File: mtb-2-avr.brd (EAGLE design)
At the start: 27 x 22 mm, 15 parts, among them IC1 MEGA8A-AU, Q1 14.745 MHz

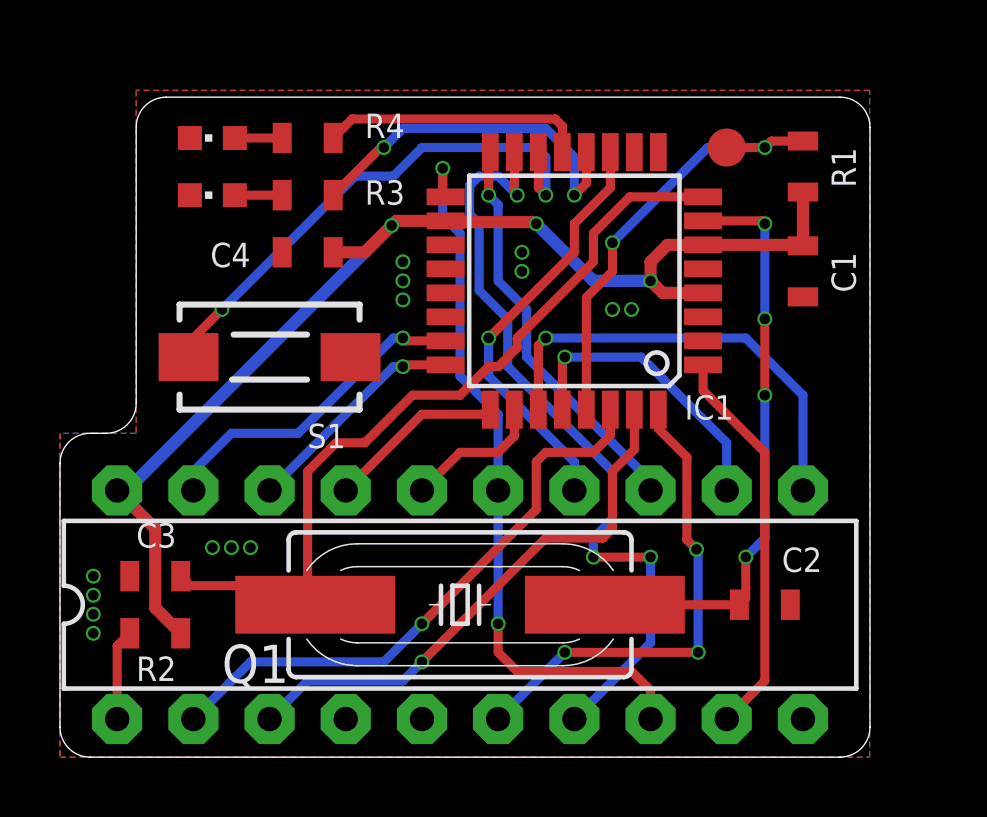
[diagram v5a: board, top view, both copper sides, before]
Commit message: Add test pad.
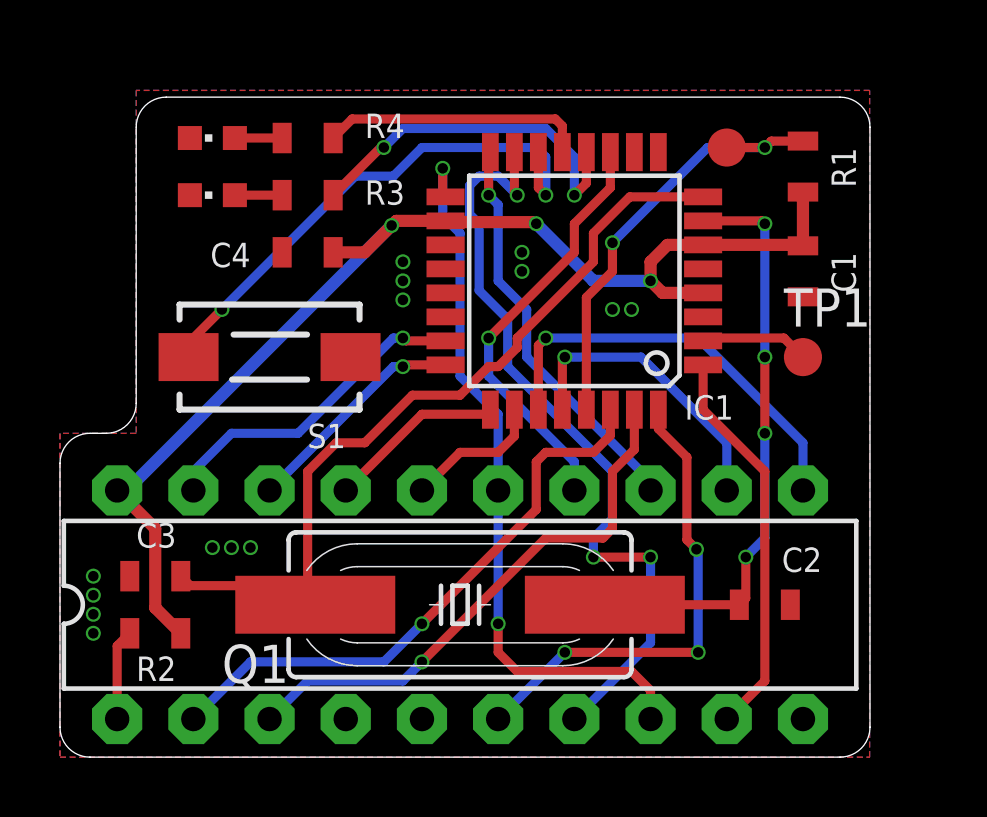
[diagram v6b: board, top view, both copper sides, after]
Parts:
- added TP1: PTR1B1,27, testpad:B1,27
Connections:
- new net TEST1: IC1.2, TP1.TP
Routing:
- net TEST1: track 0.00 -> 3.63 mm
- net SDA: track 15.0 -> 14.1 mm
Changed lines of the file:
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@@
 <layer number="25" name="tNames" color="7" fill="1" visible="no" active="yes"/>
 <layer number="26" name="bNames" color="7" fill="1" visible="no" active="yes"/>
-<layer number="27" name="tValues" color="7" fill="1" visible="yes" active="yes"/>
+<layer number="27" name="tValues" color="7" fill="1" visible="no" active="yes"/>
 <layer number="28" name="bValues" color="7" fill="1" visible="no" active="yes"/>
 <layer number="29" name="tStop" color="7" fill="3" visible="no" active="yes"/>
@@
 <attribute name="VALUE" x="9.2075" y="11.1125" size="0.8128" layer="27" rot="R180"/>
 </element>
+<element name="TP1" library="testpad" library_urn="urn:adsk.eagle:library:385" package="B1,27" package3d_urn="urn:adsk.eagle:package:27944/2" value="PTR1B1,27" x="24.765" y="13.335" smashed="yes">
+<attribute name="NAME" x="24.13" y="14.351" size="1.27" layer="25" ratio="10"/>
+<attribute name="POPULARITY" value="2" x="24.765" y="13.335" size="1.778" layer="27" display="off"/>
+<attribute name="TP_SIGNAL_NAME" value="" x="24.765" y="13.335" size="1.778" layer="27" display="off"/>
+<attribute name="VALUE" x="24.13" y="12.573" size="0.0254" layer="27"/>
+</element>
 </elements>
 <signals>
@@
 <wire x1="3.175" y1="7.62" x2="3.175" y2="4.9775" width="0.4064" layer="1"/>
 <wire x1="24.765" y1="18.835" x2="24.765" y2="17.0425" width="0.4064" layer="1"/>
-<wire x1="11.05480625" y1="17.72230625" x2="11.08875" y2="17.75625" width="0.4064" layer="16"/>
 <via x="11.05480625" y="17.72230625" extent="1-16" drill="0.35"/>
 <wire x1="2.2225" y1="8.89" x2="11.05480625" y2="17.72230625" width="0.4064" layer="16"/>
@@
 <contactref element="IC1" pad="1"/>
 <wire x1="22.225" y1="1.27" x2="23.495" y2="2.54" width="0.3048" layer="1"/>
-<wire x1="23.495" y1="2.54" x2="23.495" y2="10.16" width="0.3048" layer="1"/>
-<wire x1="21.4376" y1="13.075" x2="21.4376" y2="12.2174" width="0.3048" layer="1"/>
-<wire x1="23.495" y1="10.16" x2="21.4376" y2="12.2174" width="0.3048" layer="1"/>
+<wire x1="23.495" y1="2.54" x2="23.495" y2="9.525" width="0.3048" layer="1"/>
+<wire x1="21.4376" y1="13.075" x2="21.4376" y2="11.5824" width="0.3048" layer="1"/>
+<wire x1="23.495" y1="9.525" x2="21.4376" y2="11.5824" width="0.3048" layer="1"/>
 </signal>
 <signal name="LED_RED">
@@
 <contactref element="TORIG" pad="11"/>
 <contactref element="IC1" pad="27"/>
-<wire x1="24.765" y1="8.89" x2="24.765" y2="12.065" width="0.3048" layer="16"/>
-<wire x1="24.765" y1="12.065" x2="22.86" y2="13.97" width="0.3048" layer="16"/>
-<wire x1="22.86" y1="13.97" x2="16.1925" y2="13.97" width="0.3048" layer="16"/>
+<wire x1="24.765" y1="8.89" x2="24.765" y2="10.4775" width="0.3048" layer="16"/>
+<wire x1="24.765" y1="10.4775" x2="21.2725" y2="13.97" width="0.3048" layer="16"/>
+<wire x1="21.2725" y1="13.97" x2="16.1925" y2="13.97" width="0.3048" layer="16"/>
 <wire x1="15.945" y1="11.5824" x2="15.945" y2="13.7225" width="0.3048" layer="1"/>
 <wire x1="15.945" y1="13.7225" x2="16.1925" y2="13.97" width="0.3048" layer="1"/>
@@
 <wire x1="23.4" y1="17.875" x2="23.495" y2="17.78" width="0.3048" layer="1"/>
 <via x="23.495" y="17.78" extent="1-16" drill="0.35"/>
-<wire x1="23.495" y1="17.78" x2="23.495" y2="14.605" width="0.3048" layer="16"/>
-<via x="23.495" y="14.605" extent="1-16" drill="0.35"/>
-<wire x1="23.495" y1="14.605" x2="23.495" y2="12.065" width="0.3048" layer="1"/>
-<via x="23.495" y="12.065" extent="1-16" drill="0.35"/>
-<wire x1="23.495" y1="12.065" x2="23.495" y2="7.3025" width="0.3048" layer="16"/>
+<wire x1="23.495" y1="17.78" x2="23.495" y2="13.335" width="0.3048" layer="16"/>
+<via x="23.495" y="13.335" extent="1-16" drill="0.35"/>
+<wire x1="23.495" y1="13.335" x2="23.495" y2="10.795" width="0.3048" layer="1"/>
+<via x="23.495" y="10.795" extent="1-16" drill="0.35"/>
+<wire x1="23.495" y1="10.795" x2="23.495" y2="7.3025" width="0.3048" layer="16"/>
 <wire x1="23.495" y1="7.3025" x2="22.86" y2="6.6675" width="0.3048" layer="16"/>
 <via x="22.86" y="6.6675" extent="1-16" drill="0.35"/>
@@
 <wire x1="14.2875" y1="18.7325" x2="14.2875" y2="20.1101" width="0.3048" layer="1"/>
 <wire x1="14.2875" y1="20.1101" x2="14.345" y2="20.1676" width="0.3048" layer="1"/>
-<wire x1="14.1926" y1="20.32" x2="14.345" y2="20.1676" width="0.3048" layer="1"/>
 <wire x1="19.685" y1="9.2075" x2="15.5575" y2="13.335" width="0.3048" layer="16"/>
 <wire x1="19.685" y1="9.2075" x2="19.685" y2="8.89" width="0.3048" layer="16"/>
@@
 <wire x1="9.8425" y1="19.3675" x2="5.3975" y2="14.9225" width="0.3048" layer="16"/>
 </signal>
+<signal name="TEST1">
+<contactref element="IC1" pad="2"/>
+<contactref element="TP1" pad="TP"/>
+<wire x1="21.4376" y1="13.875" x2="21.5326" y2="13.97" width="0.3048" layer="1"/>
+<wire x1="24.13" y1="13.97" x2="24.765" y2="13.335" width="0.3048" layer="1"/>
+<wire x1="21.5326" y1="13.97" x2="24.13" y2="13.97" width="0.3048" layer="1"/>
+</signal>
 </signals>

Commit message: Add GND testpads.
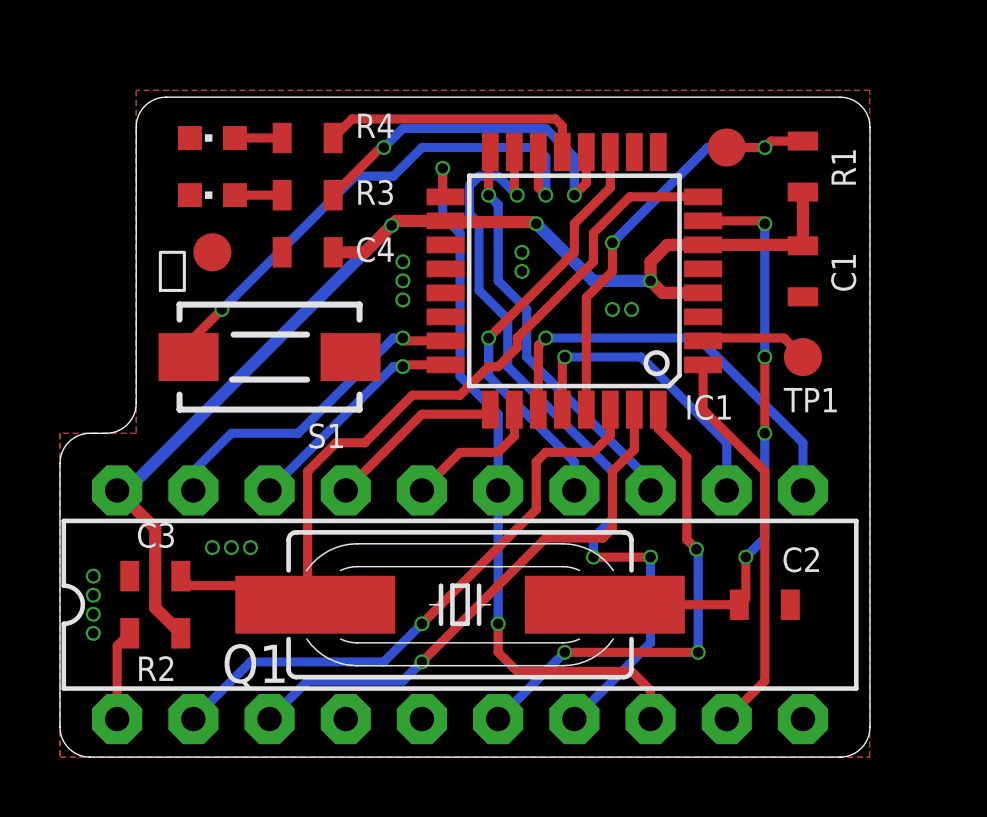
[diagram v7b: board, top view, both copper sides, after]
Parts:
- added TP2: PTR1B1,27, testpad:B1,27
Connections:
- net GND: now also TP2.TP
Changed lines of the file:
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@@
 <layer number="14" name="Route14" color="22" fill="1" visible="no" active="no"/>
 <layer number="15" name="Route15" color="23" fill="1" visible="no" active="no"/>
-<layer number="16" name="Bottom" color="4" fill="1" visible="yes" active="yes"/>
+<layer number="16" name="Bottom" color="4" fill="1" visible="no" active="yes"/>
 <layer number="17" name="Pads" color="2" fill="1" visible="yes" active="yes"/>
 <layer number="18" name="Vias" color="2" fill="1" visible="yes" active="yes"/>
-<layer number="19" name="Unrouted" color="6" fill="1" visible="yes" active="yes"/>
+<layer number="19" name="Unrouted" color="6" fill="1" visible="no" active="yes"/>
 <layer number="20" name="Dimension" color="24" fill="1" visible="yes" active="yes"/>
 <layer number="21" name="tPlace" color="7" fill="1" visible="yes" active="yes"/>
-<layer number="22" name="bPlace" color="7" fill="1" visible="yes" active="yes"/>
-<layer number="23" name="tOrigins" color="15" fill="1" visible="yes" active="yes"/>
-<layer number="24" name="bOrigins" color="15" fill="1" visible="yes" active="yes"/>
-<layer number="25" name="tNames" color="7" fill="1" visible="no" active="yes"/>
+<layer number="22" name="bPlace" color="7" fill="1" visible="no" active="yes"/>
+<layer number="23" name="tOrigins" color="15" fill="1" visible="no" active="yes"/>
+<layer number="24" name="bOrigins" color="15" fill="1" visible="no" active="yes"/>
+<layer number="25" name="tNames" color="7" fill="1" visible="yes" active="yes"/>
 <layer number="26" name="bNames" color="7" fill="1" visible="no" active="yes"/>
 <layer number="27" name="tValues" color="7" fill="1" visible="no" active="yes"/>
@@
 <layer number="44" name="Drills" color="7" fill="1" visible="no" active="yes"/>
 <layer number="45" name="Holes" color="7" fill="1" visible="no" active="yes"/>
-<layer number="46" name="Milling" color="3" fill="1" visible="yes" active="yes"/>
+<layer number="46" name="Milling" color="3" fill="1" visible="no" active="yes"/>
 <layer number="47" name="Measures" color="7" fill="1" visible="no" active="yes"/>
 <layer number="48" name="Document" color="7" fill="1" visible="no" active="yes"/>
-<layer number="49" name="Reference" color="7" fill="1" visible="yes" active="yes"/>
+<layer number="49" name="Reference" color="7" fill="1" visible="no" active="yes"/>
 <layer number="50" name="dxf" color="7" fill="1" visible="no" active="no"/>
 <layer number="51" name="tDocu" color="7" fill="1" visible="yes" active="yes"/>
-<layer number="52" name="bDocu" color="7" fill="1" visible="yes" active="yes"/>
+<layer number="52" name="bDocu" color="7" fill="1" visible="no" active="yes"/>
 <layer number="53" name="tGND_GNDA" color="7" fill="9" visible="no" active="no"/>
 <layer number="54" name="bGND_GNDA" color="1" fill="9" visible="no" active="no"/>
@@
 <text x="19.685" y="7.62" size="1.27" layer="22" rot="MR270" align="center-left">MISO</text>
 <text x="14.605" y="7.62" size="1.27" layer="22" rot="MR270" align="center-left">SCK</text>
+<text x="3.175" y="15.5575" size="1.27" layer="21">⏚</text>
 </plain>
 <attributes>
@@
 <element name="C4" library="rcl" package="C0603" value="100n" x="8.255" y="16.8275" smashed="yes" rot="R180">
 <attribute name="LCSC_PART" value="C14663" x="8.255" y="16.8275" size="1.778" layer="27" rot="R180" display="off"/>
-<attribute name="NAME" x="6.35" y="17.145" size="0.8128" layer="25" rot="R180"/>
+<attribute name="NAME" x="9.8425" y="16.51" size="0.8128" layer="25"/>
 <attribute name="VALUE" x="6.985" y="17.145" size="0.8128" layer="27" rot="R180"/>
 </element>
@@
 <element name="R3" library="rcl" package="R0603" value="10k" x="8.255" y="18.7325" smashed="yes">
 <attribute name="LCSC_PART" value="C25804" x="8.255" y="18.7325" size="1.778" layer="27" display="off"/>
-<attribute name="NAME" x="10.16" y="18.415" size="0.8128" layer="25"/>
+<attribute name="NAME" x="9.8425" y="18.415" size="0.8128" layer="25"/>
 <attribute name="VALUE" x="9.525" y="18.7325" size="0.8128" layer="27"/>
 </element>
 <element name="R4" library="rcl" package="R0603" value="1k" x="8.255" y="20.6375" smashed="yes">
 <attribute name="LCSC_PART" value="C21190" x="8.255" y="20.6375" size="1.778" layer="27" display="off"/>
-<attribute name="NAME" x="10.16" y="20.6375" size="0.8128" layer="25"/>
+<attribute name="NAME" x="9.8425" y="20.6375" size="0.8128" layer="25"/>
 <attribute name="VALUE" x="9.8425" y="20.6375" size="0.8128" layer="27"/>
 </element>
@@
 </element>
 <element name="TP1" library="testpad" library_urn="urn:adsk.eagle:library:385" package="B1,27" package3d_urn="urn:adsk.eagle:package:27944/2" value="PTR1B1,27" x="24.765" y="13.335" smashed="yes">
-<attribute name="NAME" x="24.13" y="14.351" size="1.27" layer="25" ratio="10"/>
+<attribute name="NAME" x="24.13" y="11.4935" size="0.8128" layer="25" ratio="10"/>
 <attribute name="POPULARITY" value="2" x="24.765" y="13.335" size="1.778" layer="27" display="off"/>
 <attribute name="TP_SIGNAL_NAME" value="" x="24.765" y="13.335" size="1.778" layer="27" display="off"/>
 <attribute name="VALUE" x="24.13" y="12.573" size="0.0254" layer="27"/>
+</element>
+<element name="TP2" library="testpad" library_urn="urn:adsk.eagle:library:385" package="B1,27" package3d_urn="urn:adsk.eagle:package:27944/2" value="PTR1B1,27" x="5.08" y="16.8275" smashed="yes">
+<attribute name="POPULARITY" value="2" x="5.08" y="16.8275" size="1.778" layer="27" display="off"/>
+<attribute name="TP_SIGNAL_NAME" value="" x="5.08" y="16.8275" size="1.778" layer="27" display="off"/>
+<attribute name="VALUE" x="4.445" y="16.0655" size="0.0254" layer="27"/>
 </element>
 </elements>
@@
 <via x="15.39875" y="16.8275" extent="1-16" drill="0.35"/>
 <contactref element="S1" pad="1"/>
+<contactref element="TP2" pad="TP"/>
 </signal>
 <signal name="VCC">
